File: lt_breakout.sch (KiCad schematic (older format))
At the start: 3 parts, among them J1 Conn_01x40_Male, J2 Conn_01x40_Male, U1 LicheeTang

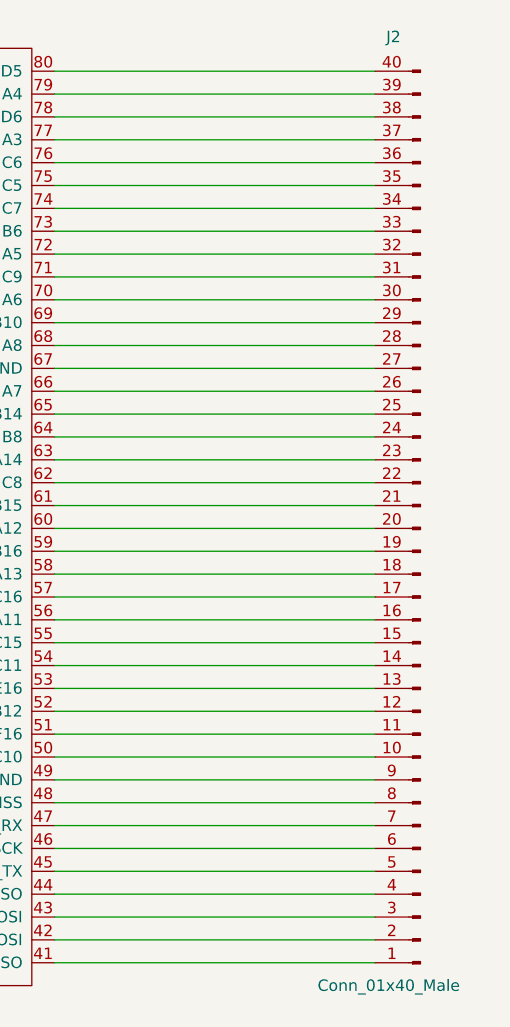
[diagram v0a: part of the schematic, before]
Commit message: Joystick net assigned.
Signed-off-by: Kali Prasad <kprasadvnsi@protonmail.com>
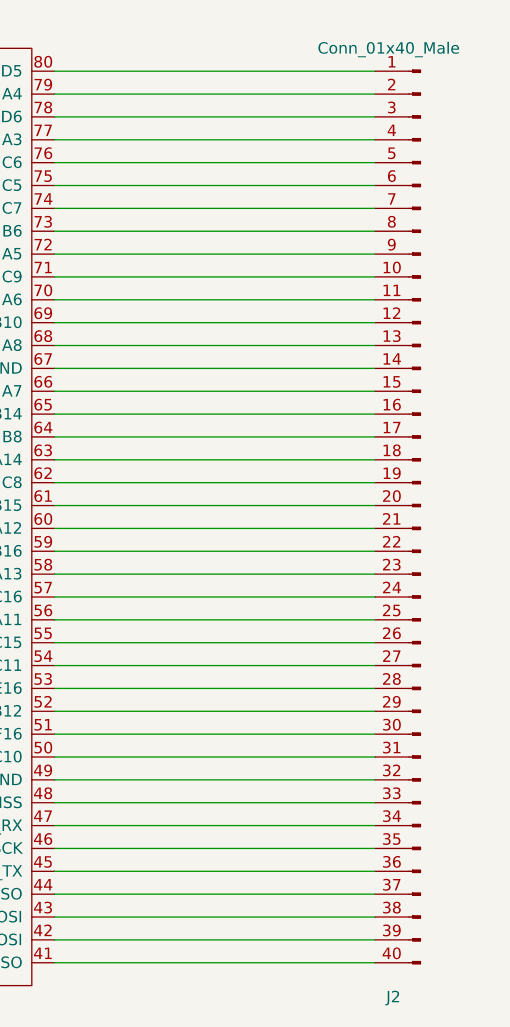
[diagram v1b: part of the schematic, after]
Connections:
- net at U1.41 (L12_PA13,SWDAT,zSPI2_MISO): now also J2.40 (Pin_40); no longer J2.1 (Pin_1)
- net at U1.42 (C12_PA7,TDI,zSPI1_MOSI): now also J2.39 (Pin_39); no longer J2.2 (Pin_2)
- net at U1.43 (J11_PA14,SWCLK,zSPI2_MOSI): now also J2.38 (Pin_38); no longer J2.3 (Pin_3)
- net at U1.44 (E14_PA6,TDO,zSPI1_MISO): now also J2.37 (Pin_37); no longer J2.4 (Pin_4)
- net at U1.45 (J13_PB6,zUART1_TX): now also J2.36 (Pin_36); no longer J2.5 (Pin_5)
- net at U1.46 (C14_PA5,TCK,zSPI1_SCK): now also J2.35 (Pin_35); no longer J2.6 (Pin_6)
- net at U1.47 (H13_PB7,zUART1_RX): now also J2.34 (Pin_34); no longer J2.7 (Pin_7)
- net at U1.48 (A15_PA4,TMS,zSPI1_NSS): now also J2.33 (Pin_33); no longer J2.8 (Pin_8)
- net at U1.49 (GND): now also J2.32 (Pin_32); no longer J2.9 (Pin_9)
- net at U1.50 (C10): now also J2.31 (Pin_31); no longer J2.10 (Pin_10)
- net at U1.51 (F16): now also J2.30 (Pin_30); no longer J2.11 (Pin_11)
- net at U1.52 (B12): now also J2.29 (Pin_29); no longer J2.12 (Pin_12)
- net at U1.53 (E16): now also J2.28 (Pin_28); no longer J2.13 (Pin_13)
- net at U1.54 (C11): now also J2.27 (Pin_27); no longer J2.14 (Pin_14)
- net at U1.55 (C15): now also J2.26 (Pin_26); no longer J2.15 (Pin_15)
- net at U1.56 (A11): now also J2.25 (Pin_25); no longer J2.16 (Pin_16)
- net at U1.57 (C16): now also J2.24 (Pin_24); no longer J2.17 (Pin_17)
- net at U1.58 (A13): now also J2.23 (Pin_23); no longer J2.18 (Pin_18)
- net at U1.59 (B16): now also J2.22 (Pin_22); no longer J2.19 (Pin_19)
- net at U1.60 (A12): now also J2.21 (Pin_21); no longer J2.20 (Pin_20)
- net at U1.61 (B15): now also J2.20 (Pin_20); no longer J2.21 (Pin_21)
- net at U1.62 (C8): now also J2.19 (Pin_19); no longer J2.22 (Pin_22)
- net at U1.63 (A14): now also J2.18 (Pin_18); no longer J2.23 (Pin_23)
- net at U1.64 (B8): now also J2.17 (Pin_17); no longer J2.24 (Pin_24)
- net at U1.65 (B14): now also J2.16 (Pin_16); no longer J2.25 (Pin_25)
- net at U1.66 (A7): now also J2.15 (Pin_15); no longer J2.26 (Pin_26)
- net at U1.67 (GND): now also J2.14 (Pin_14); no longer J2.27 (Pin_27)
- net at U1.68 (A8): now also J2.13 (Pin_13); no longer J2.28 (Pin_28)
- net at U1.69 (B10): now also J2.12 (Pin_12); no longer J2.29 (Pin_29)
- net at U1.70 (A6): now also J2.11 (Pin_11); no longer J2.30 (Pin_30)
- net at U1.71 (C9): now also J2.10 (Pin_10); no longer J2.31 (Pin_31)
- net at U1.72 (A5): now also J2.9 (Pin_9); no longer J2.32 (Pin_32)
- net at U1.73 (B6): now also J2.8 (Pin_8); no longer J2.33 (Pin_33)
- net at U1.74 (C7): now also J2.7 (Pin_7); no longer J2.34 (Pin_34)
- net at U1.75 (C5): now also J2.6 (Pin_6); no longer J2.35 (Pin_35)
- net at U1.76 (C6): now also J2.5 (Pin_5); no longer J2.36 (Pin_36)
- net at U1.77 (A3): now also J2.4 (Pin_4); no longer J2.37 (Pin_37)
- net at U1.78 (D6): now also J2.3 (Pin_3); no longer J2.38 (Pin_38)
- net at U1.79 (A4): now also J2.2 (Pin_2); no longer J2.39 (Pin_39)
- net at U1.80 (D5): now also J2.1 (Pin_1); no longer J2.40 (Pin_40)
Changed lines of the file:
@@
 L Connector:Conn_01x40_Male J2
 U 1 1 5D0F701E
-P 8400 3850
-F 0 "J2" H 8550 1700 50  0000 R CNN
-F 1 "Conn_01x40_Male" H 8850 5850 50  0000 R CNN
-F 2 "Connector_PinHeader_2.54mm:PinHeader_2x20_P2.54mm_Vertical" H 8400 3850 50  0001 C CNN
-F 3 "~" H 8400 3850 50  0001 C CNN
-	1    8400 3850
-	-1   0    0    1
+P 8400 3750
+F 0 "J2" H 8550 1600 50  0000 R CNN
+F 1 "Conn_01x40_Male" H 8850 5750 50  0000 R CNN
+F 2 "Connector_PinHeader_2.54mm:PinHeader_2x20_P2.54mm_Vertical" H 8400 3750 50  0001 C CNN
+F 3 "~" H 8400 3750 50  0001 C CNN
+	1    8400 3750
+	-1   0    0    -1
 $EndComp
 Wire Wire Line
